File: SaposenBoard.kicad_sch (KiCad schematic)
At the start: 64 parts, among them IC1 BSO220, IC2 BSO220, IC3 BSO220, IC4 BSO220, J1 Extra2ch+LED, J2 I2C, J3 Encoder1, J4 Encoder2, J5 ADC4ch, J6 Battery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

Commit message: [fix]シルク整えた
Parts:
- added D2: GS1010FL, Diode_SMD:D_SOD-123F, symbol Device:D
- Q2: value BSS138 -> IRLML6344
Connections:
- net ADC1: now also J5.5 (Pin_5); no longer J5.2 (Pin_2)
- net ADC2: now also J5.4 (Pin_4); no longer J5.3 (Pin_3)
- net ADC3: now also J5.3 (Pin_3); no longer J5.4 (Pin_4)
- net ADC4: now also J5.2 (Pin_2); no longer J5.5 (Pin_5)
- net GND: now also J1.1 (Pin_1); no longer J1.2 (Pin_2)
- net NUCLEO_LED: now also J1.2 (Pin_2); no longer J1.1 (Pin_1)
- net at BZ1.1 (-), R3.1, R5.2: now also D2.1 (K)
- net at BZ1.2 (+), Q2.3 (D), R5.1: now also D2.2 (A)
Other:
- moved on the sheet: BZ1, Q2, R3, R5, R7, R8

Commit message: [fix]ベタGND整備
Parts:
- added C17: 10u, Capacitor_SMD:C_0805_2012Metric, symbol Device:C
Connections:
- net +BATT: now also C17.2
- net ADC1: now also J5.2 (Pin_2); no longer J5.5 (Pin_5)
- net ADC2: now also J5.3 (Pin_3); no longer J5.4 (Pin_4)
- net ADC3: now also J5.4 (Pin_4); no longer J5.3 (Pin_3)
- net ADC4: now also J5.5 (Pin_5); no longer J5.2 (Pin_2)
- net GND: now also C17.1
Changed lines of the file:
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@@
     )
   )
-  (global_label "ADC2" (shape output) (at 29.21 29.21 0) (fields_autoplaced)
+  (global_label "ADC2" (shape output) (at 29.21 31.75 0) (fields_autoplaced)
     (effects (font (size 1.27 1.27)) (justify left))
-    (property "Intersheet References" "${INTERSHEET_REFS}" (id 0) (at 36.4612 29.1306 0)
+    (property "Intersheet References" "${INTERSHEET_REFS}" (id 0) (at 36.4612 31.6706 0)
       (effects (font (size 1.27 1.27)) (justify left) hide)
     )
@@
     )
   )
-  (global_label "ADC4" (shape output) (at 29.21 34.29 0) (fields_autoplaced)
+  (global_label "ADC4" (shape output) (at 29.21 26.67 0) (fields_autoplaced)
     (effects (font (size 1.27 1.27)) (justify left))
-    (property "Intersheet References" "${INTERSHEET_REFS}" (id 0) (at 36.4612 34.2106 0)
+    (property "Intersheet References" "${INTERSHEET_REFS}" (id 0) (at 36.4612 26.5906 0)
       (effects (font (size 1.27 1.27)) (justify left) hide)
     )
@@
     )
   )
-  (global_label "ADC1" (shape output) (at 29.21 26.67 0) (fields_autoplaced)
+  (global_label "ADC1" (shape output) (at 29.21 34.29 0) (fields_autoplaced)
     (effects (font (size 1.27 1.27)) (justify left))
-    (property "Intersheet References" "${INTERSHEET_REFS}" (id 0) (at 36.4612 26.5906 0)
+    (property "Intersheet References" "${INTERSHEET_REFS}" (id 0) (at 36.4612 34.2106 0)
       (effects (font (size 1.27 1.27)) (justify left) hide)
     )
@@
     )
   )
-  (global_label "ADC3" (shape output) (at 29.21 31.75 0) (fields_autoplaced)
+  (global_label "ADC3" (shape output) (at 29.21 29.21 0) (fields_autoplaced)
     (effects (font (size 1.27 1.27)) (justify left))
-    (property "Intersheet References" "${INTERSHEET_REFS}" (id 0) (at 36.4612 31.6706 0)
+    (property "Intersheet References" "${INTERSHEET_REFS}" (id 0) (at 36.4612 29.1306 0)
       (effects (font (size 1.27 1.27)) (justify left) hide)
     )
@@
     (pin "1")
     (pin "2")
+  )
+  (symbol (lib_id "power:+BATT") (at 160.02 158.75 0) (unit 1)
+    (in_bom yes) (on_board yes) (fields_autoplaced)
+    (property "Reference" "#PWR041" (id 0) (at 160.02 162.56 0)
+      (effects (font (size 1.27 1.27)) hide)
+    )
+    (property "Value" "+BATT" (id 1) (at 160.02 153.67 0))
+    (property "Footprint" "" (id 2) (at 160.02 158.75 0)
+      (effects (font (size 1.27 1.27)) hide)
+    )
+    (property "Datasheet" "" (id 3) (at 160.02 158.75 0)
+      (effects (font (size 1.27 1.27)) hide)
+    )
+    (pin "1")
   )
   (symbol (lib_id "Symbols:BSO220") (at 138.43 180.34 0) (unit 1)
@@
     (pin "2")
   )
+  (symbol (lib_name "GND_1") (lib_id "power:GND") (at 160.02 166.37 0) (unit 1)
+    (in_bom yes) (on_board yes) (fields_autoplaced)
+    (property "Reference" "#PWR042" (id 0) (at 160.02 172.72 0)
+      (effects (font (size 1.27 1.27)) hide)
+    )
+    (property "Value" "GND" (id 1) (at 160.02 171.45 0))
+    (property "Footprint" "" (id 2) (at 160.02 166.37 0)
+      (effects (font (size 1.27 1.27)) hide)
+    )
+    (property "Datasheet" "" (id 3) (at 160.02 166.37 0)
+      (effects (font (size 1.27 1.27)) hide)
+    )
+    (pin "1")
+  )
   (symbol (lib_id "power:GND") (at 266.7 44.45 0) (unit 1)
     (in_bom yes) (on_board yes) (fields_autoplaced)
@@
   (symbol (lib_id "Device:C_Polarized") (at 114.3 163.83 0) (unit 1)
     (in_bom yes) (on_board yes)
-    (property "Reference" "C16" (id 0) (at 111.76 160.02 0)
+    (property "Reference" "C16" (id 0) (at 110.49 160.02 0)
       (effects (font (size 1.27 1.27)) (justify left))
     )
@@
   (symbol (lib_id "Device:C") (at 109.22 163.83 180) (unit 1)
     (in_bom yes) (on_board yes)
-    (property "Reference" "C15" (id 0) (at 107.95 160.02 0))
+    (property "Reference" "C15" (id 0) (at 106.68 160.02 0))
     (property "Value" "10u" (id 1) (at 111.76 166.37 0))
     (property "Footprint" "Capacitor_SMD:C_0805_2012Metric" (id 2) (at 108.2548 160.02 0)
@@
     )
     (property "Datasheet" "~" (id 3) (at 38.1 73.66 0)
+      (effects (font (size 1.27 1.27)) hide)
+    )
+    (pin "1")
+    (pin "2")
+  )
+  (symbol (lib_id "Device:C") (at 160.02 162.56 180) (unit 1)
+    (in_bom yes) (on_board yes)
+    (property "Reference" "C17" (id 0) (at 157.48 158.75 0))
+    (property "Value" "10u" (id 1) (at 162.56 165.1 0))
+    (property "Footprint" "Capacitor_SMD:C_0805_2012Metric" (id 2) (at 159.0548 158.75 0)
+      (effects (font (size 1.27 1.27)) hide)
+    )
+    (property "Datasheet" "~" (id 3) (at 160.02 162.56 0)
       (effects (font (size 1.27 1.27)) hide)
     )
@@
       (reference "#PWR040") (unit 1) (value "GND") (footprint "")
     )
+    (path "/055c508c-3b1d-418a-a809-398b6f637be4"
+      (reference "#PWR041") (unit 1) (value "+BATT") (footprint "")
+    )
+    (path "/2490f256-c87e-4a39-b7d9-20bfb1e78b0a"
+      (reference "#PWR042") (unit 1) (value "GND") (footprint "")
+    )
     (path "/81921910-1553-4bf4-a413-1642e4c1e2f1"
       (reference "#PWR0102") (unit 1) (value "+BATT") (footprint "")
@@
       (reference "C16") (unit 1) (value "100u") (footprint "Capacitor_SMD:C_Elec_6.3x7.7")
     )
+    (path "/873b996d-e157-4eca-8d41-174033615b4e"
+      (reference "C17") (unit 1) (value "10u") (footprint "Capacitor_SMD:C_0805_2012Metric")
+    )
     (path "/bd45fd34-dad9-4840-b033-05972db02fc5"

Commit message: [update]チェックもらった
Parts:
- removed D1: ESD9B3.3ST5G, Diode_SMD:D_SOD-923, symbol Diode:ESD9B3.3ST5G
- added D1: MMSZ4684-TP, Diode_SMD:D_SOD-123, symbol Device:D_Zener
- C1, C16, C6: footprint Capacitor_SMD:C_Elec_6.3x7.7 -> Capacitor_THT:CP_Radial_D5.0mm_P2.50mm
- renumbered J5 to J1, J1 to J2, J2 to J5, U2 to U1, U4 to U2, U1 to U4
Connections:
- net GND: now also D1.2 (A)
- net VBAT: now also D1.1 (K)
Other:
- moved on the sheet: C17, J3, J4, R22, R23

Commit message: [update]終わった
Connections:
- net ADC1: now also U4.4_12 (PA_0); no longer U4.4_10 (PA_3)
- net ADC2: now also U4.4_10 (PA_3); no longer U4.4_9 (PA_4)
- net ADC3: now also U4.3_9 (PB_1); no longer U4.4_8 (PA_5)
- net ADC4: now also U4.3_6 (PB_0); no longer U4.4_7 (PA_6)
- net ENC1_1: now also U4.4_11 (PA_1); no longer U4.3_12 (PA_8)
- net ENC1_2: now also U4.4_8 (PA_5); no longer U4.3_1 (PA_9)
- net ENC2_1: now also U4.4_7 (PA_6); no longer U4.3_14 (PB_5)
- net ENC2_2: now also U4.4_6 (PA_7); no longer U4.3_15 (PB_4)
- net Extra1: now also J2.2 (Pin_2), U4.3_15 (PB_4); no longer J2.3 (Pin_3), U4.3_9 (PB_1)
- net Extra2: now also J2.3 (Pin_3), U4.3_14 (PB_5); no longer J2.4 (Pin_4), U4.4_6 (PA_7)
- net MOT1_IN2: now also U4.3_1 (PA_9); no longer U4.3_13 (PA_11)
- net MOT2_IN1: now also U4.3_13 (PA_11); no longer U4.4_12 (PA_0)
- net MOT2_IN2: now also U4.3_12 (PA_8); no longer U4.4_11 (PA_1)
- net NUCLEO_LED: now also J2.4 (Pin_4); no longer J2.2 (Pin_2)
- net VBAT: now also U4.4_9 (PA_4); no longer U4.3_6 (PB_0)

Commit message: a
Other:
- moved on the sheet: BZ1, D2, R3, R5
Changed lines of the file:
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@@
   (junction (at 121.92 60.96) (diameter 0) (color 0 0 0 0)
   )
-  (junction (at 73.66 58.42) (diameter 0) (color 0 0 0 0)
+  (junction (at 73.66 55.88) (diameter 0) (color 0 0 0 0)
   )
   (junction (at 148.59 171.45) (diameter 0) (color 0 0 0 0)
@@
   (junction (at 38.1 139.7) (diameter 0) (color 0 0 0 0)
   )
+  (junction (at 68.58 55.88) (diameter 0) (color 0 0 0 0)
+  )
   (junction (at 55.88 111.76) (diameter 0) (color 0 0 0 0)
   )
@@
   )
   (junction (at 120.65 30.48) (diameter 0) (color 0 0 0 0)
-  )
-  (junction (at 68.58 58.42) (diameter 0) (color 0 0 0 0)
   )
   (junction (at 115.57 63.5) (diameter 0) (color 0 0 0 0)
@@
     (stroke (width 0) (type default) (color 0 0 0 0))
   )
-  (wire (pts (xy 62.23 67.31) (xy 62.23 68.58))
+  (wire (pts (xy 62.23 66.04) (xy 62.23 68.58))
     (stroke (width 0) (type default) (color 0 0 0 0))
   )
@@
     (stroke (width 0) (type default) (color 0 0 0 0))
   )
-  (wire (pts (xy 62.23 58.42) (xy 68.58 58.42))
+  (wire (pts (xy 62.23 55.88) (xy 68.58 55.88))
     (stroke (width 0) (type default) (color 0 0 0 0))
   )
@@
     (stroke (width 0) (type default) (color 0 0 0 0))
   )
-  (wire (pts (xy 73.66 57.15) (xy 73.66 58.42))
+  (wire (pts (xy 73.66 54.61) (xy 73.66 55.88))
     (stroke (width 0) (type default) (color 0 0 0 0))
   )
@@
     (stroke (width 0) (type default) (color 0 0 0 0))
   )
-  (wire (pts (xy 73.66 66.04) (xy 73.66 68.58))
+  (wire (pts (xy 73.66 64.77) (xy 73.66 68.58))
     (stroke (width 0) (type default) (color 0 0 0 0))
   )
@@
     (stroke (width 0) (type default) (color 0 0 0 0))
   )
+  (wire (pts (xy 68.58 55.88) (xy 68.58 58.42))
+    (stroke (width 0) (type default) (color 0 0 0 0))
+  )
   (wire (pts (xy 91.44 127) (xy 125.73 127))
     (stroke (width 0) (type default) (color 0 0 0 0))
@@
     (stroke (width 0) (type default) (color 0 0 0 0))
   )
-  (wire (pts (xy 68.58 58.42) (xy 73.66 58.42))
+  (wire (pts (xy 68.58 55.88) (xy 73.66 55.88))
     (stroke (width 0) (type default) (color 0 0 0 0))
   )
@@
     (stroke (width 0) (type default) (color 0 0 0 0))
   )
-  (wire (pts (xy 68.58 67.31) (xy 68.58 68.58))
+  (wire (pts (xy 68.58 66.04) (xy 68.58 68.58))
     (stroke (width 0) (type default) (color 0 0 0 0))
   )
@@
     (stroke (width 0) (type default) (color 0 0 0 0))
   )
-  (wire (pts (xy 73.66 58.42) (xy 73.66 60.96))
+  (wire (pts (xy 73.66 55.88) (xy 73.66 59.69))
     (stroke (width 0) (type default) (color 0 0 0 0))
   )
@@
     (stroke (width 0) (type default) (color 0 0 0 0))
   )
-  (wire (pts (xy 73.66 48.26) (xy 73.66 49.53))
+  (wire (pts (xy 73.66 45.72) (xy 73.66 46.99))
     (stroke (width 0) (type default) (color 0 0 0 0))
   )
@@
     (stroke (width 0) (type default) (color 0 0 0 0))
   )
-  (wire (pts (xy 62.23 59.69) (xy 62.23 58.42))
+  (wire (pts (xy 62.23 58.42) (xy 62.23 55.88))
     (stroke (width 0) (type default) (color 0 0 0 0))
   )
@@
   )
   (wire (pts (xy 66.04 114.3) (xy 63.5 114.3))
-    (stroke (width 0) (type default) (color 0 0 0 0))
-  )
-  (wire (pts (xy 68.58 59.69) (xy 68.58 58.42))
     (stroke (width 0) (type default) (color 0 0 0 0))
   )
@@
     (pin "1")
   )
-  (symbol (lib_id "Device:R") (at 73.66 53.34 180) (unit 1)
-    (in_bom yes) (on_board yes)
-    (property "Reference" "R3" (id 0) (at 68.58 52.07 0)
+  (symbol (lib_id "Device:R") (at 73.66 50.8 180) (unit 1)
+    (in_bom yes) (on_board yes)
+    (property "Reference" "R3" (id 0) (at 68.58 49.53 0)
       (effects (font (size 1.27 1.27)) (justify right))
     )
-    (property "Value" "470" (id 1) (at 73.66 53.34 90))
-    (property "Footprint" "Resistor_SMD:R_0603_1608Metric" (id 2) (at 75.438 53.34 90)
-      (effects (font (size 1.27 1.27)) hide)
-    )
-    (property "Datasheet" "~" (id 3) (at 73.66 53.34 0)
+    (property "Value" "470" (id 1) (at 73.66 50.8 90))
+    (property "Footprint" "Resistor_SMD:R_0603_1608Metric" (id 2) (at 75.438 50.8 90)
+      (effects (font (size 1.27 1.27)) hide)
+    )
+    (property "Datasheet" "~" (id 3) (at 73.66 50.8 0)
       (effects (font (size 1.27 1.27)) hide)
     )
@@
     (pin "2")
   )
-  (symbol (lib_id "Device:Buzzer") (at 76.2 63.5 0) (unit 1)
-    (in_bom yes) (on_board yes)
-    (property "Reference" "BZ1" (id 0) (at 77.47 59.69 0)
+  (symbol (lib_id "Device:Buzzer") (at 76.2 62.23 0) (unit 1)
+    (in_bom yes) (on_board yes)
+    (property "Reference" "BZ1" (id 0) (at 77.47 58.42 0)
       (effects (font (size 1.27 1.27)) (justify left))
     )
-    (property "Value" "Buzzer" (id 1) (at 76.2 68.58 0)
+    (property "Value" "Buzzer" (id 1) (at 76.2 67.31 0)
       (effects (font (size 1.27 1.27)) (justify left))
     )
-    (property "Footprint" "Footprints:PKM13EPYH4000-A0" (id 2) (at 75.565 60.96 90)
-      (effects (font (size 1.27 1.27)) hide)
-    )
-    (property "Datasheet" "~" (id 3) (at 75.565 60.96 90)
+    (property "Footprint" "Footprints:PKM13EPYH4000-A0" (id 2) (at 75.565 59.69 90)
+      (effects (font (size 1.27 1.27)) hide)
+    )
+    (property "Datasheet" "~" (id 3) (at 75.565 59.69 90)
       (effects (font (size 1.27 1.27)) hide)
     )
@@
     (pin "8")
   )
-  (symbol (lib_id "power:+BATT") (at 73.66 48.26 0) (unit 1)
-    (in_bom yes) (on_board yes) (fields_autoplaced)
-    (property "Reference" "#PWR015" (id 0) (at 73.66 52.07 0)
-      (effects (font (size 1.27 1.27)) hide)
-    )
-    (property "Value" "+BATT" (id 1) (at 73.66 43.18 0))
-    (property "Footprint" "" (id 2) (at 73.66 48.26 0)
-      (effects (font (size 1.27 1.27)) hide)
-    )
-    (property "Datasheet" "" (id 3) (at 73.66 48.26 0)
+  (symbol (lib_id "power:+BATT") (at 73.66 45.72 0) (unit 1)
+    (in_bom yes) (on_board yes) (fields_autoplaced)
+    (property "Reference" "#PWR015" (id 0) (at 73.66 49.53 0)
+      (effects (font (size 1.27 1.27)) hide)
+    )
+    (property "Value" "+BATT" (id 1) (at 73.66 40.64 0))
+    (property "Footprint" "" (id 2) (at 73.66 45.72 0)
+      (effects (font (size 1.27 1.27)) hide)
+    )
+    (property "Datasheet" "" (id 3) (at 73.66 45.72 0)
       (effects (font (size 1.27 1.27)) hide)
     )
@@
     (pin "1")
   )
-  (symbol (lib_id "Device:R") (at 68.58 63.5 180) (unit 1)
-    (in_bom yes) (on_board yes)
-    (property "Reference" "R5" (id 0) (at 66.04 59.69 0)
+  (symbol (lib_id "Device:R") (at 68.58 62.23 180) (unit 1)
+    (in_bom yes) (on_board yes)
+    (property "Reference" "R5" (id 0) (at 66.04 58.42 0)
       (effects (font (size 1.27 1.27)) (justify right))
     )
-    (property "Value" "1k" (id 1) (at 68.58 63.5 90))
-    (property "Footprint" "Resistor_SMD:R_0603_1608Metric" (id 2) (at 70.358 63.5 90)
-      (effects (font (size 1.27 1.27)) hide)
-    )
-    (property "Datasheet" "~" (id 3) (at 68.58 63.5 0)
+    (property "Value" "1k" (id 1) (at 68.58 62.23 90))
+    (property "Footprint" "Resistor_SMD:R_0603_1608Metric" (id 2) (at 70.358 62.23 90)
+      (effects (font (size 1.27 1.27)) hide)
+    )
+    (property "Datasheet" "~" (id 3) (at 68.58 62.23 0)
       (effects (font (size 1.27 1.27)) hide)
     )
@@
   (symbol (lib_id "Device:C") (at 38.1 181.61 0) (unit 1)
     (in_bom yes) (on_board yes)
-    (property "Reference" "C12" (id 0) (at 36.83 179.07 0))
+    (property "Reference" "C12" (id 0) (at 35.56 179.07 0))
     (property "Value" "470p" (id 1) (at 40.64 184.15 0))
     (property "Footprint" "Capacitor_SMD:C_0603_1608Metric" (id 2) (at 39.0652 185.42 0)
@@
     (pin "1")
   )
-  (symbol (lib_id "Device:D") (at 62.23 63.5 270) (unit 1)
-    (in_bom yes) (on_board yes)
-    (property "Reference" "D2" (id 0) (at 59.69 59.69 90)
+  (symbol (lib_id "Device:D") (at 62.23 62.23 270) (unit 1)
+    (in_bom yes) (on_board yes)
+    (property "Reference" "D2" (id 0) (at 59.69 58.42 90)
       (effects (font (size 1.27 1.27)) (justify left))
     )
-    (property "Value" "GS1010FL" (id 1) (at 64.77 58.42 0)
+    (property "Value" "GS1010FL" (id 1) (at 64.77 57.15 0)
       (effects (font (size 1.27 1.27)) (justify left))
     )
-    (property "Footprint" "Diode_SMD:D_SOD-123F" (id 2) (at 62.23 63.5 0)
-      (effects (font (size 1.27 1.27)) hide)
-    )
-    (property "Datasheet" "~" (id 3) (at 62.23 63.5 0)
-      (effects (font (size 1.27 1.27)) hide)
-    )
-    (property "Field4" "NP" (id 4) (at 60.96 67.31 90))
-    (pin "1")
-    (pin "2")
+    (property "Footprint" "Diode_SMD:D_SOD-123F" (id 2) (at 62.23 62.23 0)
+      (effects (font (size 1.27 1.27)) hide)
+    )
+    (property "Datasheet" "~" (id 3) (at 62.23 62.23 0)
+      (effects (font (size 1.27 1.27)) hide)
+    )
+    (property "Field4" "NP" (id 4) (at 60.96 66.04 90))
+    (pin "1")
+    (pin "2")

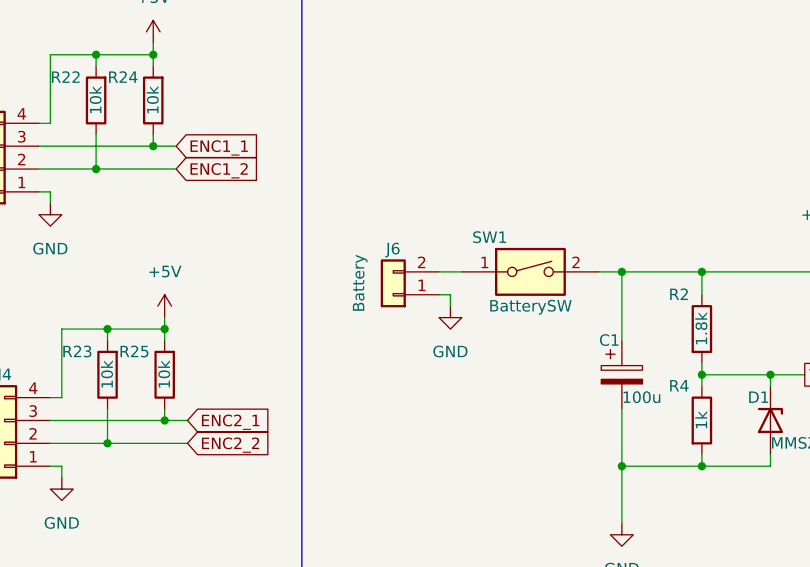
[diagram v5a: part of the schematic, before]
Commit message: [fix]コネクタの向きを修正
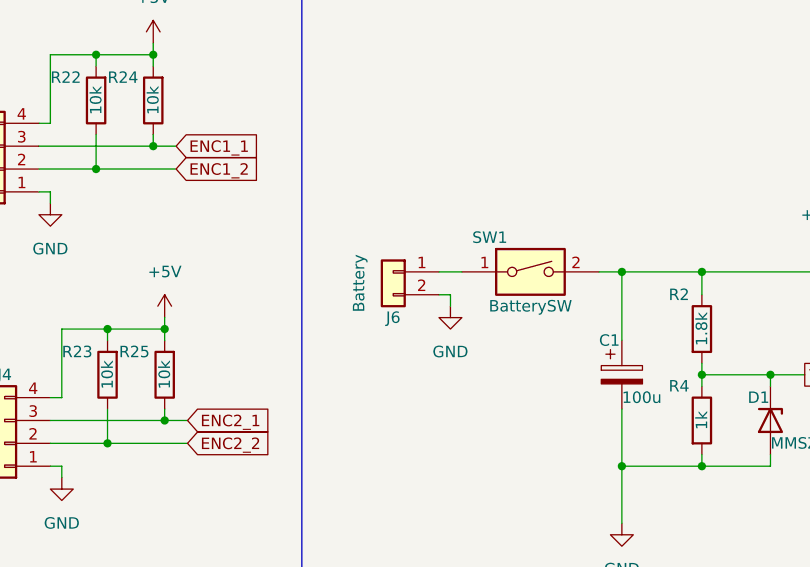
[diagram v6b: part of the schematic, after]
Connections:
- net GND: now also J6.2 (Pin_2); no longer J6.1 (Pin_1)
- net at SW1.1: now also J6.1 (Pin_1); no longer J6.2 (Pin_2)
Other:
- moved on the sheet: J6
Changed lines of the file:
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@@
+    (stroke (width 0) (type default) (color 0 0 0 0))
+  )
+  (wire (pts (xy 152.4 46.99) (xy 153.67 46.99))
     (stroke (width 0) (type default) (color 0 0 0 0))
   )
@@
   )
   (wire (pts (xy 172.72 44.45) (xy 172.72 52.07))
-    (stroke (width 0) (type default) (color 0 0 0 0))
-  )
-  (wire (pts (xy 152.4 46.99) (xy 153.67 46.99))
     (stroke (width 0) (type default) (color 0 0 0 0))
   )
@@
     (pin "2")
   )
-  (symbol (lib_id "Connector_Generic:Conn_01x02") (at 147.32 46.99 180) (unit 1)
-    (in_bom yes) (on_board yes)
-    (property "Reference" "J6" (id 0) (at 147.32 41.91 0))
+  (symbol (lib_id "Connector_Generic:Conn_01x02") (at 147.32 44.45 0) (mirror y) (unit 1)
+    (in_bom yes) (on_board yes)
+    (property "Reference" "J6" (id 0) (at 147.32 49.53 0))
     (property "Value" "Battery" (id 1) (at 143.51 45.72 90))
-    (property "Footprint" "Footprints:IL-G_2P" (id 2) (at 147.32 46.99 0)
-      (effects (font (size 1.27 1.27)) hide)
-    )
-    (property "Datasheet" "~" (id 3) (at 147.32 46.99 0)
-      (effects (font (size 1.27 1.27)) hide)
-    )
+    (property "Footprint" "Footprints:IL-G_2P" (id 2) (at 147.32 44.45 0)
+      (effects (font (size 1.27 1.27)) hide)
+    )
+    (property "Datasheet" "~" (id 3) (at 147.32 44.45 0)
+      (effects (font (size 1.27 1.27)) hide)
+    )

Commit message: [update]BOM出力
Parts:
- C13, C14, C4, C7: value 0.1u -> 100n
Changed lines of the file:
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@@
     (in_bom yes) (on_board yes)
     (property "Reference" "C13" (id 0) (at 92.71 160.02 90))
-    (property "Value" "0.1u" (id 1) (at 100.33 162.56 90))
+    (property "Value" "100n" (id 1) (at 100.33 162.56 90))
     (property "Footprint" "Capacitor_SMD:C_0603_1608Metric" (id 2) (at 100.33 160.3248 0)
       (effects (font (size 1.27 1.27)) hide)
@@
     (in_bom yes) (on_board yes)
     (property "Reference" "C14" (id 0) (at 92.71 167.64 90))
-    (property "Value" "0.1u" (id 1) (at 100.33 170.18 90))
+    (property "Value" "100n" (id 1) (at 100.33 170.18 90))
     (property "Footprint" "Capacitor_SMD:C_0603_1608Metric" (id 2) (at 100.33 167.9448 0)
       (effects (font (size 1.27 1.27)) hide)
@@
     (in_bom yes) (on_board yes)
     (property "Reference" "C4" (id 0) (at 92.71 113.03 90))
-    (property "Value" "0.1u" (id 1) (at 100.33 115.57 90))
+    (property "Value" "100n" (id 1) (at 100.33 115.57 90))
     (property "Footprint" "Capacitor_SMD:C_0603_1608Metric" (id 2) (at 100.33 113.3348 0)
       (effects (font (size 1.27 1.27)) hide)
@@
     (in_bom yes) (on_board yes)
     (property "Reference" "C7" (id 0) (at 92.71 120.65 90))
-    (property "Value" "0.1u" (id 1) (at 100.33 123.19 90))
+    (property "Value" "100n" (id 1) (at 100.33 123.19 90))
     (property "Footprint" "Capacitor_SMD:C_0603_1608Metric" (id 2) (at 100.33 120.9548 0)
       (effects (font (size 1.27 1.27)) hide)
@@
     )
     (path "/15695f51-b913-4e0e-800e-852e07677b29"
-      (reference "C4") (unit 1) (value "0.1u") (footprint "Capacitor_SMD:C_0603_1608Metric")
+      (reference "C4") (unit 1) (value "100n") (footprint "Capacitor_SMD:C_0603_1608Metric")
     )
     (path "/30a2f918-55a5-46d2-a42a-3d005f5078e6"
@@
     )
     (path "/53a48944-52cf-4353-8060-7f63f7c629d6"
-      (reference "C7") (unit 1) (value "0.1u") (footprint "Capacitor_SMD:C_0603_1608Metric")
+      (reference "C7") (unit 1) (value "100n") (footprint "Capacitor_SMD:C_0603_1608Metric")
     )
     (path "/cf08b498-581b-48f1-ab49-b460fcae54dc"
@@
     )
     (path "/046716bc-3e25-49f7-b93d-a0c3a842205d"
-      (reference "C13") (unit 1) (value "0.1u") (footprint "Capacitor_SMD:C_0603_1608Metric")
+      (reference "C13") (unit 1) (value "100n") (footprint "Capacitor_SMD:C_0603_1608Metric")
     )
     (path "/0d58b576-4f91-4294-85a5-772722818ef7"
-      (reference "C14") (unit 1) (value "0.1u") (footprint "Capacitor_SMD:C_0603_1608Metric")
+      (reference "C14") (unit 1) (value "100n") (footprint "Capacitor_SMD:C_0603_1608Metric")
     )
     (path "/51015f58-976e-4957-b1ac-0a5c13ab17be"
